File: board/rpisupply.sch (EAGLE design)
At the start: 21 parts, among them IC1 ATTINY45-20SU, Q1 IRF7416, SW1 SCHURTER-LSH-1301.x, X1 MINI-USB, X2 AVR-ISP-6-EDGE

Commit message: Change frame in schematics
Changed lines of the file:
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@@
 <?xml version="1.0" encoding="utf-8"?>
 <!DOCTYPE eagle SYSTEM "eagle.dtd">
-<eagle version="6.3">
+<eagle version="7.4.0">
 <drawing>
 <settings>
@@
 <instance part="Q1" gate="G$1" x="81.28" y="109.22" rot="R90"/>
 <instance part="GND5" gate="1" x="48.26" y="99.06"/>
-<instance part="R1" gate="G$1" x="43.18" y="104.14"/>
+<instance part="R1" gate="G$1" x="43.18" y="104.14" smashed="yes">
+<attribute name="NAME" x="39.37" y="105.6386" size="1.778" layer="95"/>
+<attribute name="VALUE" x="45.212" y="105.664" size="1.778" layer="96"/>
+</instance>
 <instance part="GND7" gate="1" x="127" y="99.06"/>
 <instance part="H1" gate="G$1" x="7.62" y="5.08"/>
@@
 <instance part="SW1" gate="G$1" x="119.38" y="53.34" smashed="yes" rot="R90">
 <attribute name="NAME" x="116.6114" y="48.26" size="1.778" layer="95" rot="R90"/>
-<attribute name="VALUE" x="127.127" y="42.2275" size="1.778" layer="96" rot="R90"/>
+<attribute name="VALUE" x="129.667" y="42.2275" size="1.778" layer="96" rot="R90"/>
 </instance>
 </instances>

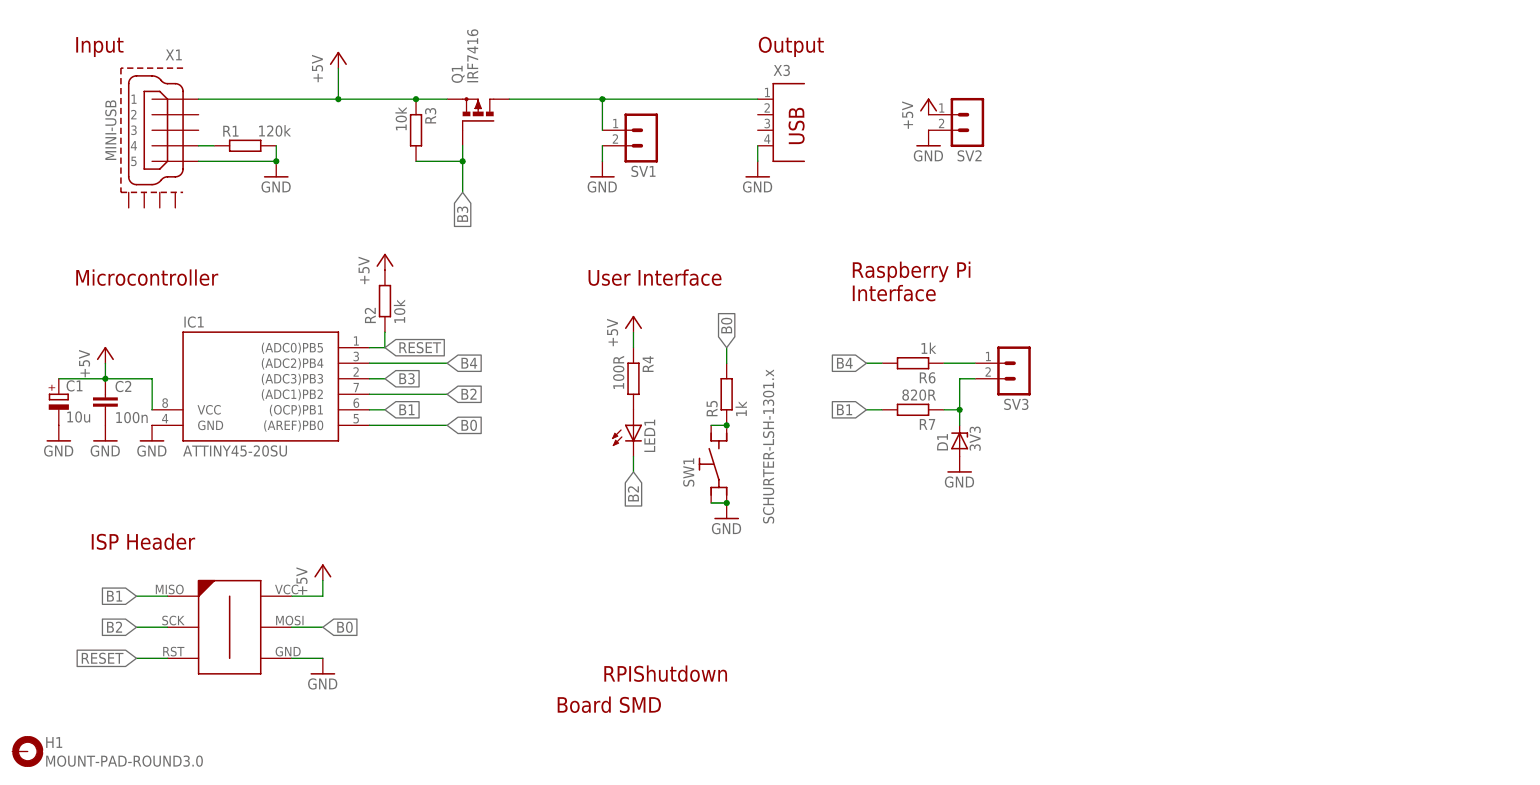
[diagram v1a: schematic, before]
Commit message: add bidirectional levelshifter
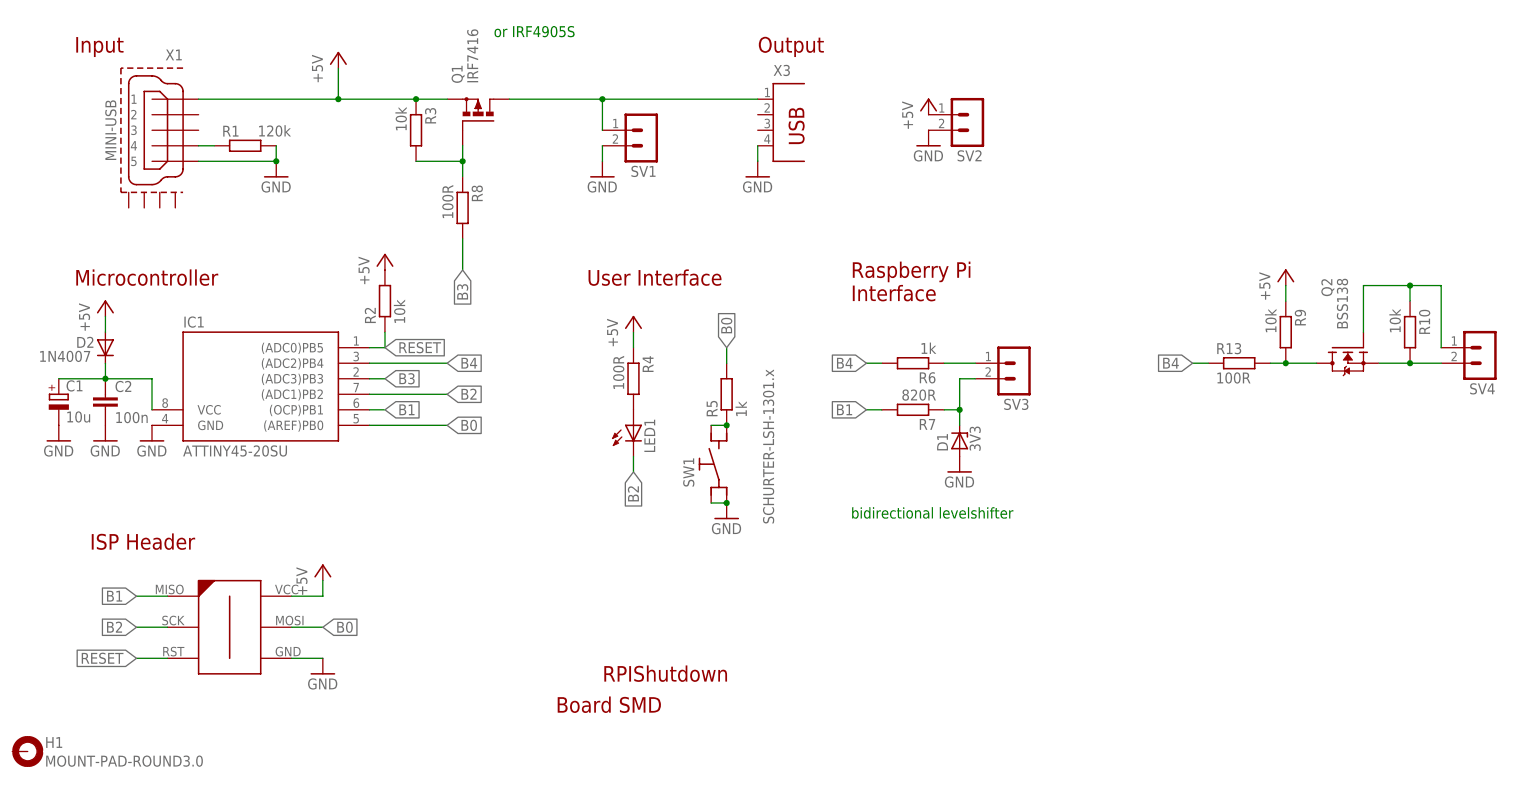
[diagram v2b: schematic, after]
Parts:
- added D2: 1N4007, diode:DIODE-MELF-MLL41
- added Q2: BSS138, transistor-fet:BSS138BSS138
- added R10, R9: 10k, rcl:R-EU_R0805
- added R13, R8: 100R, rcl:R-EU_R0805
- added SV4: (no value), con-lstb:MA02-1R
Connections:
- new net N$12: Q2.D, R13.2, R9.2
- new net N$6: Q1.G, R3.2, R8.1
- new net N$7: C1.+, C2.1, D2.C, IC1.VCC
- new net N$8: Q2.G, R10.1, SV4.1
- new net N$9: Q2.S, R10.2, SV4.2
- net +5V: now also D2.A, R9.1; no longer C1.+, C2.1, IC1.VCC
- net B3: now also R8.2; no longer Q1.G, R3.2
- net B4: now also R13.1
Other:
- note added: "bidirectional levelshifter"
- note added: "or IRF4905S"

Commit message: add components for next version
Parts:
- removed SV4: (no value), con-lstb:MA02-1R
- added Q3: BSS138, transistor-fet:BSS138BSS138
- added Q4: IRF4905S, transistor-fet:IRF4905S
- added R11, R12: 10k, rcl:R-EU_R0805
- added R14: 100R, rcl:R-EU_R0805
- added SV5: (no value), con-lstb:MA03-1R
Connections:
- new net N$10: Q3.D, R11.2, R14.2
- new net N$11: Q3.S, R12.2, SV5.3
- net +5V: now also R11.1
- net B0: now also R13.1
- net B2: now also R14.1
- net B4: no longer R13.1
- net N$8: now also Q3.G, R12.1, SV5.1; no longer SV4.1
- net N$9: now also SV5.2; no longer SV4.2
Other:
- note added: "I2C PB0 PB2"
- note added: "add fuse"
- moved on the sheet: R10, R13, R9
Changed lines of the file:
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@@
 <part name="P+6" library="supply1" deviceset="+5V" device=""/>
 <part name="R13" library="rcl" deviceset="R-EU_" device="R0805" value="100R"/>
-<part name="SV4" library="con-lstb" deviceset="MA02-1R" device=""/>
+<part name="SV5" library="con-lstb" deviceset="MA03-1R" device=""/>
+<part name="R11" library="rcl" deviceset="R-EU_" device="R0805" value="10k"/>
+<part name="R12" library="rcl" deviceset="R-EU_" device="R0805" value="10k"/>
+<part name="R14" library="rcl" deviceset="R-EU_" device="R0805" value="100R"/>
+<part name="P+8" library="supply1" deviceset="+5V" device=""/>
+<part name="Q3" library="transistor-fet" deviceset="BSS138" device="BSS138" value="BSS138"/>
+<part name="Q4" library="transistor-fet" deviceset="IRF4905S" device=""/>
 </parts>
 <sheets>
@@
 <text x="83.82" y="121.92" size="1.778" layer="91">or IRF4905S</text>
 <text x="142.24" y="43.18" size="1.778" layer="91">bidirectional levelshifter</text>
+<text x="200.66" y="53.34" size="1.778" layer="91">I2C PB0 PB2</text>
+<text x="149.86" y="121.92" size="1.778" layer="91">add fuse</text>
 </plain>
 <instances>
@@
 </instance>
 <instance part="Q2" gate="G$1" x="223.52" y="71.12" rot="MR270"/>
-<instance part="R9" gate="G$1" x="213.36" y="73.66" rot="R270"/>
-<instance part="R10" gate="G$1" x="233.68" y="73.66" rot="R270"/>
+<instance part="R9" gate="G$1" x="213.36" y="76.2" rot="R270"/>
+<instance part="R10" gate="G$1" x="233.68" y="76.2" rot="R270"/>
 <instance part="P+6" gate="1" x="213.36" y="83.82"/>
-<instance part="R13" gate="G$1" x="205.74" y="68.58"/>
-<instance part="SV4" gate="G$1" x="246.38" y="71.12" rot="R180"/>
+<instance part="R13" gate="G$1" x="198.12" y="68.58"/>
+<instance part="SV5" gate="G$1" x="251.46" y="68.58" rot="R180"/>
+<instance part="R11" gate="G$1" x="205.74" y="76.2" rot="R270"/>
+<instance part="R12" gate="G$1" x="238.76" y="76.2" rot="R270"/>
+<instance part="R14" gate="G$1" x="198.12" y="60.96"/>
+<instance part="P+8" gate="1" x="205.74" y="83.82"/>
+<instance part="Q3" gate="G$1" x="226.06" y="63.5" rot="MR270"/>
+<instance part="Q4" gate="G$1" x="106.68" y="119.38"/>
 </instances>
 <busses>
@@
 <pinref part="R9" gate="G$1" pin="1"/>
 <pinref part="P+6" gate="1" pin="+5V"/>
-<wire x1="213.36" y1="81.28" x2="213.36" y2="78.74" width="0.1524" layer="91"/>
+</segment>
+<segment>
+<pinref part="R11" gate="G$1" pin="1"/>
+<pinref part="P+8" gate="1" pin="+5V"/>
 </segment>
 </net>
@@
 <label x="144.78" y="68.58" size="1.778" layer="95" rot="R180" xref="yes"/>
 </segment>
-<segment>
-<pinref part="R13" gate="G$1" pin="1"/>
-<wire x1="200.66" y1="68.58" x2="198.12" y2="68.58" width="0.1524" layer="91"/>
-<label x="198.12" y="68.58" size="1.778" layer="95" rot="R180" xref="yes"/>
-</segment>
 </net>
 <net name="B3" class="0">
@@
 <label x="106.68" y="50.8" size="1.778" layer="95" rot="R270" xref="yes"/>
 </segment>
+<segment>
+<pinref part="R14" gate="G$1" pin="1"/>
+<wire x1="193.04" y1="60.96" x2="190.5" y2="60.96" width="0.1524" layer="91"/>
+<label x="190.5" y="60.96" size="1.778" layer="95" rot="R180" xref="yes"/>
+</segment>
 </net>
 <net name="B1" class="0">
@@
 <wire x1="121.92" y1="68.58" x2="121.92" y2="71.12" width="0.1524" layer="91"/>
 <label x="121.92" y="71.12" size="1.778" layer="95" rot="R90" xref="yes"/>
+</segment>
+<segment>
+<pinref part="R13" gate="G$1" pin="1"/>
+<wire x1="193.04" y1="68.58" x2="190.5" y2="68.58" width="0.1524" layer="91"/>
+<label x="190.5" y="68.58" size="1.778" layer="95" rot="R180" xref="yes"/>
 </segment>
 </net>
@@
 <pinref part="Q2" gate="G$1" pin="G"/>
 <wire x1="226.06" y1="73.66" x2="226.06" y2="81.28" width="0.1524" layer="91"/>
-<wire x1="226.06" y1="81.28" x2="233.68" y2="81.28" width="0.1524" layer="91"/>
+<wire x1="226.06" y1="81.28" x2="228.6" y2="81.28" width="0.1524" layer="91"/>
 <pinref part="R10" gate="G$1" pin="1"/>
-<wire x1="233.68" y1="81.28" x2="233.68" y2="78.74" width="0.1524" layer="91"/>
+<wire x1="228.6" y1="81.28" x2="233.68" y2="81.28" width="0.1524" layer="91"/>
 <wire x1="233.68" y1="81.28" x2="238.76" y2="81.28" width="0.1524" layer="91"/>
 <junction x="233.68" y="81.28"/>
-<wire x1="238.76" y1="71.12" x2="238.76" y2="81.28" width="0.1524" layer="91"/>
-<pinref part="SV4" gate="G$1" pin="1"/>
+<wire x1="238.76" y1="81.28" x2="243.84" y2="81.28" width="0.1524" layer="91"/>
+<wire x1="243.84" y1="71.12" x2="243.84" y2="81.28" width="0.1524" layer="91"/>
+<pinref part="SV5" gate="G$1" pin="1"/>
+<pinref part="R12" gate="G$1" pin="1"/>
+<junction x="238.76" y="81.28"/>
+<pinref part="Q3" gate="G$1" pin="G"/>
+<wire x1="228.6" y1="66.04" x2="228.6" y2="81.28" width="0.1524" layer="91"/>
+<junction x="228.6" y="81.28"/>
+</segment>
+</net>
+<net name="N$12" class="0">
+<segment>
+<pinref part="R9" gate="G$1" pin="2"/>
+<pinref part="R13" gate="G$1" pin="2"/>
+<wire x1="203.2" y1="68.58" x2="213.36" y2="68.58" width="0.1524" layer="91"/>
+<wire x1="213.36" y1="68.58" x2="213.36" y2="71.12" width="0.1524" layer="91"/>
+<pinref part="Q2" gate="G$1" pin="D"/>
+<wire x1="218.44" y1="68.58" x2="213.36" y2="68.58" width="0.1524" layer="91"/>
+<junction x="213.36" y="68.58"/>
 </segment>
 </net>
 <net name="N$9" class="0">
 <segment>
+<pinref part="SV5" gate="G$1" pin="2"/>
 <pinref part="Q2" gate="G$1" pin="S"/>
-<wire x1="228.6" y1="68.58" x2="233.68" y2="68.58" width="0.1524" layer="91"/>
+<wire x1="243.84" y1="68.58" x2="233.68" y2="68.58" width="0.1524" layer="91"/>
 <pinref part="R10" gate="G$1" pin="2"/>
+<wire x1="233.68" y1="68.58" x2="228.6" y2="68.58" width="0.1524" layer="91"/>
+<wire x1="233.68" y1="71.12" x2="233.68" y2="68.58" width="0.1524" layer="91"/>
 <junction x="233.68" y="68.58"/>
-<wire x1="233.68" y1="68.58" x2="238.76" y2="68.58" width="0.1524" layer="91"/>
-<pinref part="SV4" gate="G$1" pin="2"/>
-</segment>
-</net>
-<net name="N$12" class="0">
-<segment>
-<pinref part="Q2" gate="G$1" pin="D"/>
-<pinref part="R9" gate="G$1" pin="2"/>
-<wire x1="218.44" y1="68.58" x2="213.36" y2="68.58" width="0.1524" layer="91"/>
-<pinref part="R13" gate="G$1" pin="2"/>
-<wire x1="210.82" y1="68.58" x2="213.36" y2="68.58" width="0.1524" layer="91"/>
-<junction x="213.36" y="68.58"/>
-</segment>
-</net>
+</segment>
+</net>
+<net name="N$10" class="0">
+<segment>
+<pinref part="R11" gate="G$1" pin="2"/>
+<pinref part="R14" gate="G$1" pin="2"/>
+<wire x1="205.74" y1="71.12" x2="205.74" y2="60.96" width="0.1524" layer="91"/>
+<wire x1="205.74" y1="60.96" x2="203.2" y2="60.96" width="0.1524" layer="91"/>
+<pinref part="Q3" gate="G$1" pin="D"/>
+<wire x1="220.98" y1="60.96" x2="205.74" y2="60.96" width="0.1524" layer="91"/>
+<junction x="205.74" y="60.96"/>
+</segment>
+</net>
+<net name="N$11" class="0">
+<segment>
+<pinref part="R12" gate="G$1" pin="2"/>
+<pinref part="Q3" gate="G$1" pin="S"/>
+<wire x1="238.76" y1="71.12" x2="238.76" y2="60.96" width="0.1524" layer="91"/>
+<wire x1="238.76" y1="60.96" x2="231.14" y2="60.96" width="0.1524" layer="91"/>
+<pinref part="SV5" gate="G$1" pin="3"/>
+<wire x1="243.84" y1="66.04" x2="243.84" y2="60.96" width="0.1524" layer="91"/>
+<wire x1="243.84" y1="60.96" x2="238.76" y2="60.96" width="0.1524" layer="91"/>
+<junction x="238.76" y="60.96"/>
+</segment>
+</net>
